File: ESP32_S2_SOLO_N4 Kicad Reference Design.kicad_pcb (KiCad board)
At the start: 2 copper layers, 95 x 110 mm, 50 parts, among them J2 USB_C_Receptacle_USB2.0, Q1 NPN, SW1 Reset, SW2 Boot, SW3 SW_SPDT, SW5 SW_SPDT, U1 ESP32-S2-SOLO, U10 LM339DR, U2 LD1117S33TR_SOT223, U3 LM339DR

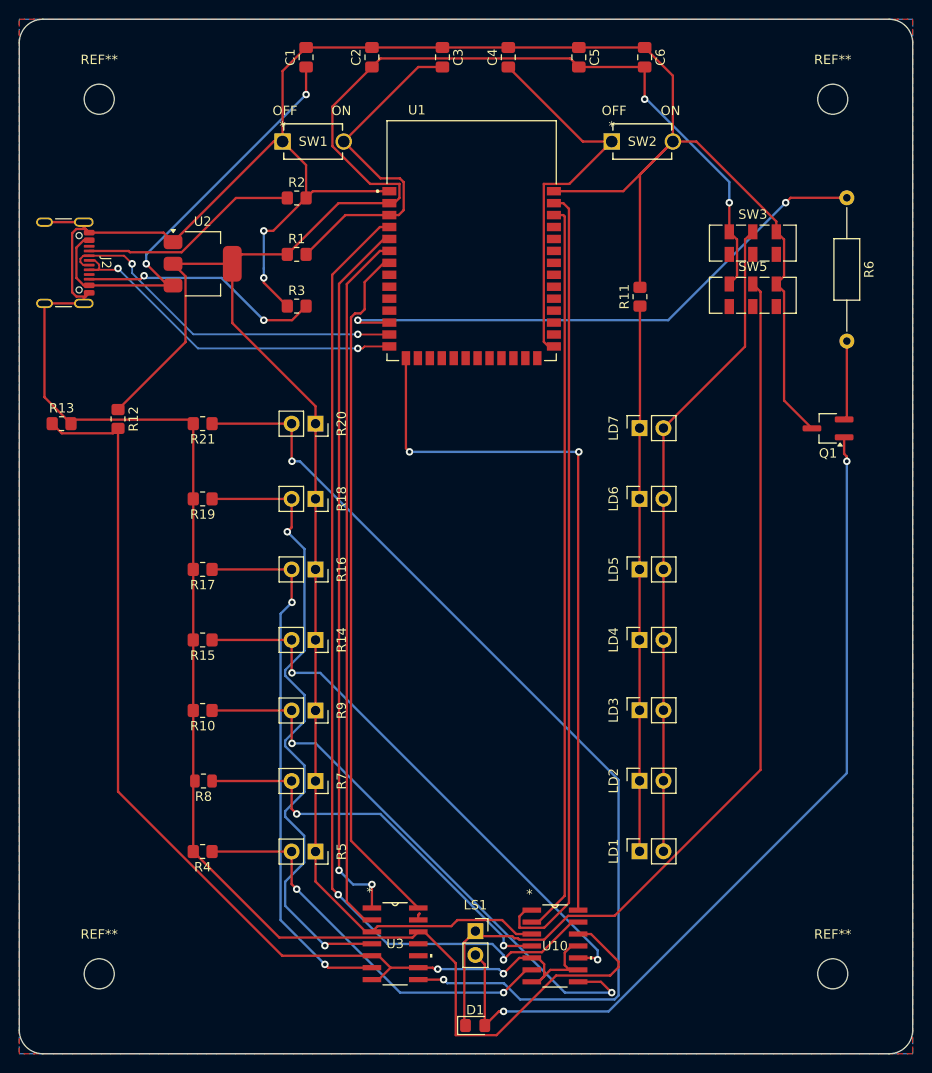
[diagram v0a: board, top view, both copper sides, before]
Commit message: I2S speaker and ESD protection schematic and footprints added
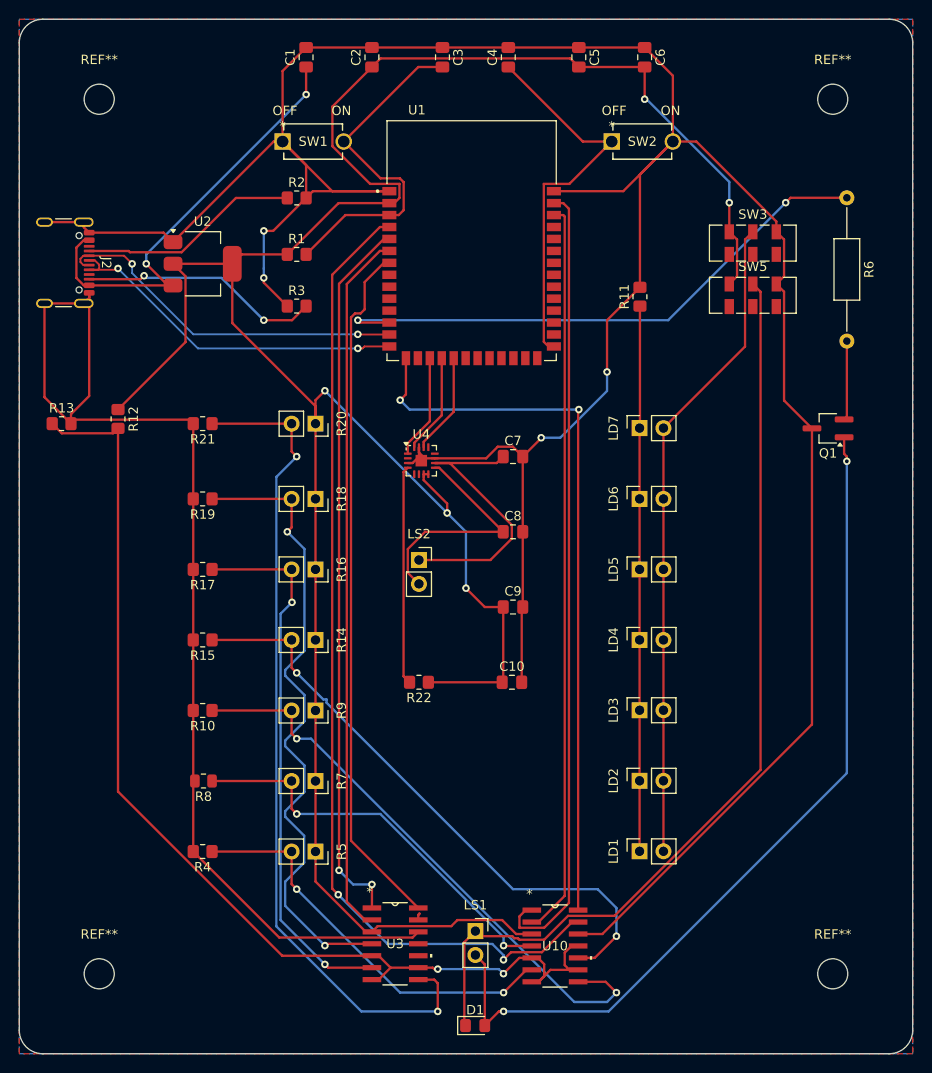
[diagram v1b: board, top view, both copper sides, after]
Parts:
- added C10: 0.1uF, Capacitor_SMD:C_0805_2012Metric_Pad1.18x1.45mm_HandSolder, F.Cu at (148.9, 110.0)
- added C7: 220pF, Capacitor_SMD:C_0805_2012Metric_Pad1.18x1.45mm_HandSolder, F.Cu at (149.0, 86.0)
- added C8: 220pF, Capacitor_SMD:C_0805_2012Metric_Pad1.18x1.45mm_HandSolder, F.Cu at (149.0, 94.0)
- added C9: 10uF, Capacitor_SMD:C_0805_2012Metric_Pad1.18x1.45mm_HandSolder, F.Cu at (149.0, 102.0)
- added LS2: Speaker, Connector_PinSocket_2.54mm:PinSocket_1x02_P2.54mm_Vertical, F.Cu at (139.0, 97.0)
- added R22: 1M, Resistor_SMD:R_0805_2012Metric_Pad1.20x1.40mm_HandSolder, F.Cu at (139.0, 110.0)
- added U4: MAX98357A, Package_DFN_QFN:TQFN-16-1EP_3x3mm_P0.5mm_EP1.23x1.23mm, F.Cu at (139.2, 86.4)
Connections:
- U1 pad 17: unconnected-(U1-GPIO9/TOUCH9/ADC1_CH8/FSPIHD-Pad17) -> /I2S1
- U1 pad 18: unconnected-(U1-GPIO10/TOUCH10/ADC1_CH9/FSPICS0/FSPIIO4-Pad18) -> /I2S2
- U1 pad 19: unconnected-(U1-GPIO11/TOUCH11/ADC2_CH0/FSPID/FSPIIO5-Pad19) -> /I2S3
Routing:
- net GND: track 347.5 -> 454.9 mm, vias 2 -> 4
- net +3.3V: track 219.5 -> 277.0 mm, vias 2 -> 5
- net Net-(U4-OUTN): track 0.00 -> 31.8 mm
- net Net-(U4-OUTP): track 0.00 -> 25.2 mm
- net Net-(U4-~{SD_MODE}): track 0.00 -> 23.3 mm
- net /D6: track 106.5 -> 89.2 mm
- net /I2S1: track 0.00 -> 11.1 mm
- net /I2S3: track 0.00 -> 10.8 mm
- net /I2S2: track 0.00 -> 10.7 mm
- net /D3: track 59.8 -> 64.8 mm
- net /D2: track 61.0 -> 62.2 mm
- net /A2: track 76.9 -> 77.4 mm

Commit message: Final project submission
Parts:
- added D2: SMAJ5.0CA, Diode_SMD:D_0805_2012Metric_Pad1.15x1.40mm_HandSolder, F.Cu at (104.0, 122.0)
- added D3: SMAJ5.0CA, Diode_SMD:D_0805_2012Metric_Pad1.15x1.40mm_HandSolder, F.Cu at (104.0, 114.0)
- added D4: D, Diode_SMD:D_0805_2012Metric_Pad1.15x1.40mm_HandSolder, F.Cu at (104.0, 98.0)
- added D5: D_Schottky, Diode_SMD:D_0805_2012Metric_Pad1.15x1.40mm_HandSolder, F.Cu at (104.0, 106.0)
- added F1: Polyfuse, Diode_SMD:D_0805_2012Metric_Pad1.15x1.40mm_HandSolder, F.Cu at (104.0, 90.0)
- added TP1: TestPoint, TestPoint:TestPoint_Plated_Hole_D2.0mm, F.Cu at (116.0, 47.0)
- added TP2: TestPoint, TestPoint:TestPoint_Plated_Hole_D2.0mm, F.Cu at (172.0, 48.0)
- added TP3: TestPoint, TestPoint:TestPoint_Plated_Hole_D2.0mm, F.Cu at (117.0, 141.0)
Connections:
- C1 pad 1: +5V -> /ESD Protected 5V
- U2 pad 3: +5V -> /ESD Protected 5V
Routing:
- net /ESD Protected 5V: track 0.00 -> 115.4 mm, vias 0 -> 4
- net /D+: track 38.4 -> 97.6 mm, vias 2 -> 3
- net /D-: track 38.5 -> 92.0 mm, vias 2 -> 3
- net GND: track 454.9 -> 494.2 mm, vias 4 -> 6
- net +3.3V: track 277.0 -> 288.0 mm, vias 5 -> 6
- net +5V: track 47.3 -> 55.5 mm, vias 2 -> 4
- net Net-(D4-A): track 0.00 -> 8.00 mm
- net /D3: track 64.8 -> 67.6 mm
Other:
- board text added: "Conor"
- board text added: "HOPE"
- board text added: "Harris Thai Achyut S. Chebiyam Ishir Garg"
- board text added: "Laser Harp"
